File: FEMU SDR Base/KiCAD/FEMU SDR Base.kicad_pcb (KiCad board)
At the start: 4 copper layers, 164.8 x 186.6 mm, 71 parts, among them P1 Battery, P10 PWM2, P11 PWM3, P12 PWM4, P13 PWM1, P14 PWM2, P15 PWM3, P16 PWM4, P17 12V, P18 GND, P19 12V, P2 SDR_Shield_1, P20 GND, P21 S0GND, P22 S1GND, P23 S0DN, P24 S1DN, P25 S0DP, P26 S1DP, P27 PWM0, P28 PWM5, P29 PWM6, P3 SDR_Shield_2, P30 PWM7, P31 PWM0, P32 PWM5, P33 PWM6, P34 PWM7, P35 Battery, P4 12V, P5 GND, P6 12V, P7 GND, P8 Raspi_Power_Shield, P9 PWM1, U1 TPS562209, U2 LP38858-LDO, U3 LP38858-LDO, U4 7833, U5 7833

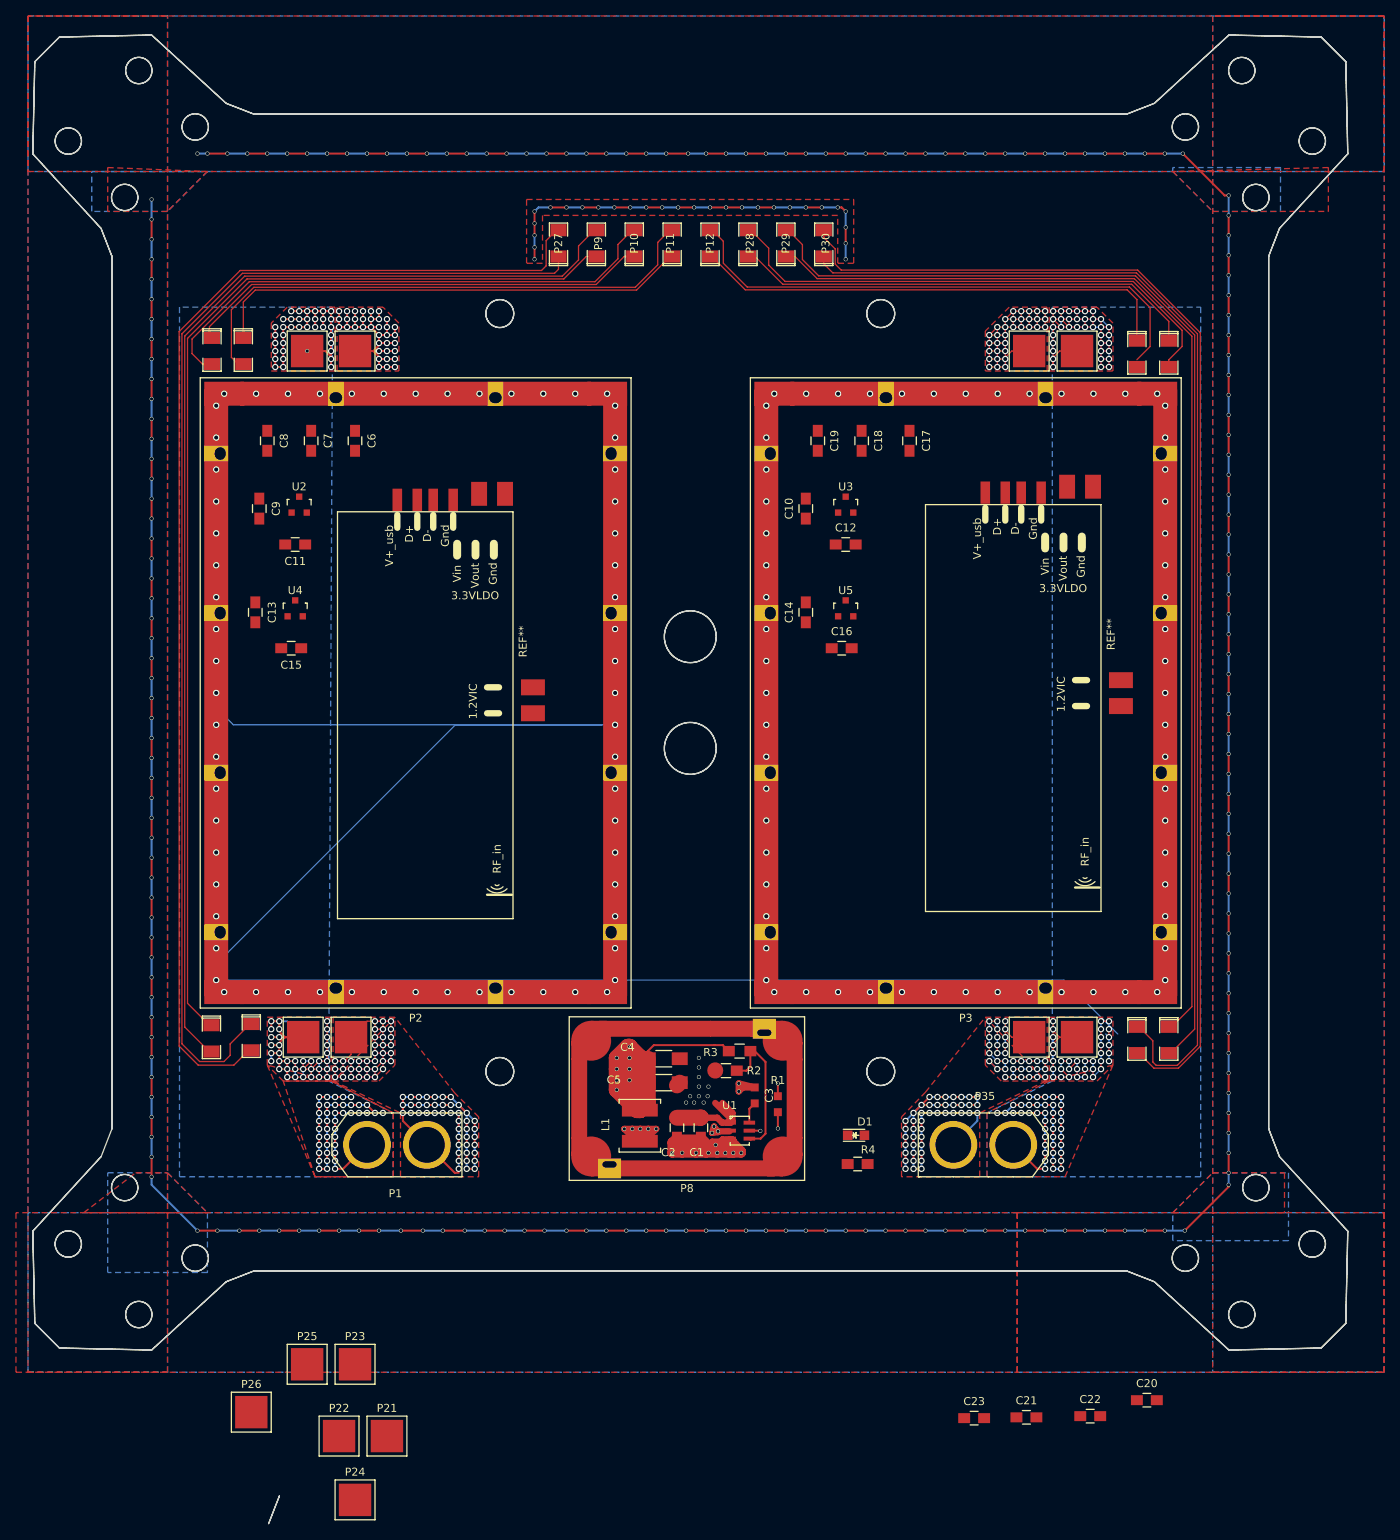
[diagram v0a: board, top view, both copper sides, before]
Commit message: Added esc mounts, power headers and usb headers
Signed-off-by: hardiepienaar <hardiepienaar@gmail.com>
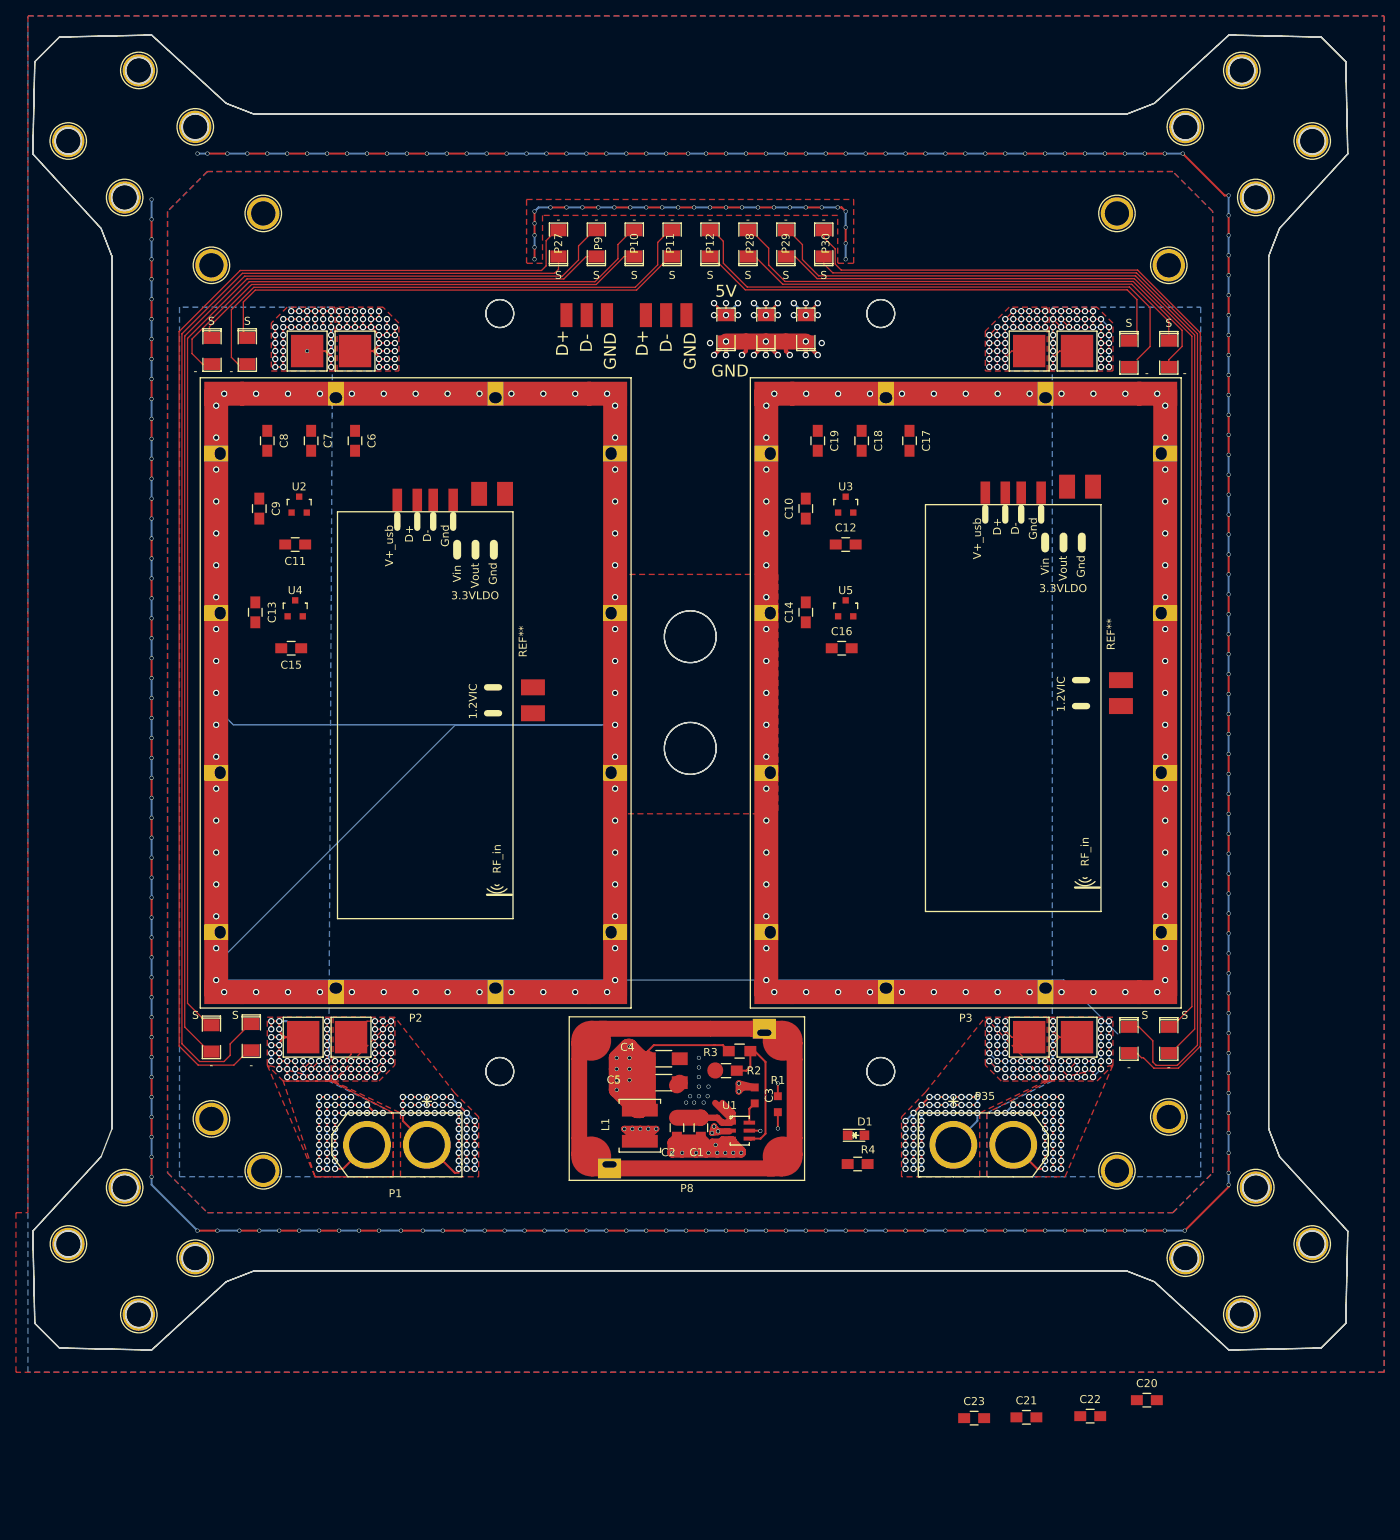
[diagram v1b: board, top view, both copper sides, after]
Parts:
- removed P23: S0DN, SMD_Packages:1Pin
- removed P24: S1DN, SMD_Packages:1Pin
- removed P25: S0DP, SMD_Packages:1Pin
- removed P26: S1DP, SMD_Packages:1Pin
- added M1: M1, Connect:1pin, F.Cu at (13.6, 146.6)
- added M10: M1, Connect:1pin, F.Cu at (6.55, 15.4)
- added M11: M1, Connect:1pin, F.Cu at (22.5, 13.7)
- added M12: M1, Connect:1pin, F.Cu at (13.6, 22.5)
- added M13: M1, Connect:1pin, F.Cu at (153.7, 6.58)
- added M14: M1, Connect:1pin, F.Cu at (146.6, 13.7)
- added M15: M1, Connect:1pin, F.Cu at (162.5, 15.4)
- added M16: M1, Connect:1pin, F.Cu at (155.4, 22.5)
- added M2: M1, Connect:1pin, F.Cu at (155.4, 146.6)
- added M3: M1, Connect:1pin, F.Cu at (162.5, 153.7)
- added M4: M1, Connect:1pin, F.Cu at (153.7, 162.5)
- added M5: M1, Connect:1pin, F.Cu at (146.6, 155.4)
- added M6: M1, Connect:1pin, F.Cu at (6.58, 153.7)
- added M7: M1, Connect:1pin, F.Cu at (15.4, 162.5)
- added M8: M1, Connect:1pin, F.Cu at (22.5, 155.4)
- added M9: M1, Connect:1pin, F.Cu at (15.4, 6.58)
- added P36: RPi, SMD_Packages:SMD-1206_Pol, F.Cu at (99.0, 38.9)
- added P37: PXH, SMD_Packages:SMD-1206_Pol, F.Cu at (94.0, 38.9)
- added P38: Rx, SMD_Packages:SMD-1206_Pol, F.Cu at (89.0, 38.9)
- added REF**: 1pin, Connect:1pin, F.Cu at (24.5, 31.0)
- added REF**: 1pin, Connect:1pin, F.Cu at (24.5, 138.0)
- added REF**: 1pin, Connect:1pin, F.Cu at (31.0, 24.5)
- added REF**: 1pin, Connect:1pin, F.Cu at (144.5, 31.0)
- added REF**: 1pin, Connect:1pin, F.Cu at (138.0, 24.5)
- added REF**: 1pin, Connect:1pin, F.Cu at (144.5, 137.8)
- added REF**: 1pin, Connect:1pin, F.Cu at (138.0, 144.5)
- added REF**: 1pin, Connect:1pin, F.Cu at (31.0, 144.5)
- P21: value S0GND -> SDR0; footprint SMD_Packages:1Pin -> Misc footprints:USB
- P22: value S1GND -> SDR1; footprint SMD_Packages:1Pin -> Misc footprints:USB
- moved P22 146.4 mm to (81.5, 37.2)
- moved P21 142.7 mm to (71.5, 37.2)
- moved P16 1.00 mm to (139.5, 42.1)
- moved P34 1.00 mm to (139.5, 128.1)
- moved P15 0.50 mm to (29.0, 41.8)
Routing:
- net +5V: track 95.7 -> 220.8 mm, vias 8 -> 22
- net GND: track 1642.1 -> 1668.3 mm, vias 587 -> 605
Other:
- board size 164.8 x 186.6 mm -> 164.8 x 164.8 mm
- board text added: "+"
- board text added: "-"
- board text added: "5V"
- board text added: "Connect 5V line (Antheun) Add feedthroughs (Antheun) Add usb isolation (Antheun) Finish SDR layouts (Antheun) Add MESA logo Add FEMU logo Add Description Add Rev and date Add Sneaky signitures Add mechanical drawings to silkscreen"
- board text added: "D+"
- board text added: "D-"
- board text added: "GND"
- board text added: "S"
- board text removed: "Add raspi power Add pixhawk pwr Add feedthroughs Add usb isolation Add esc wire strap mounts Add SMA grounding rings Add arm grounding rings"

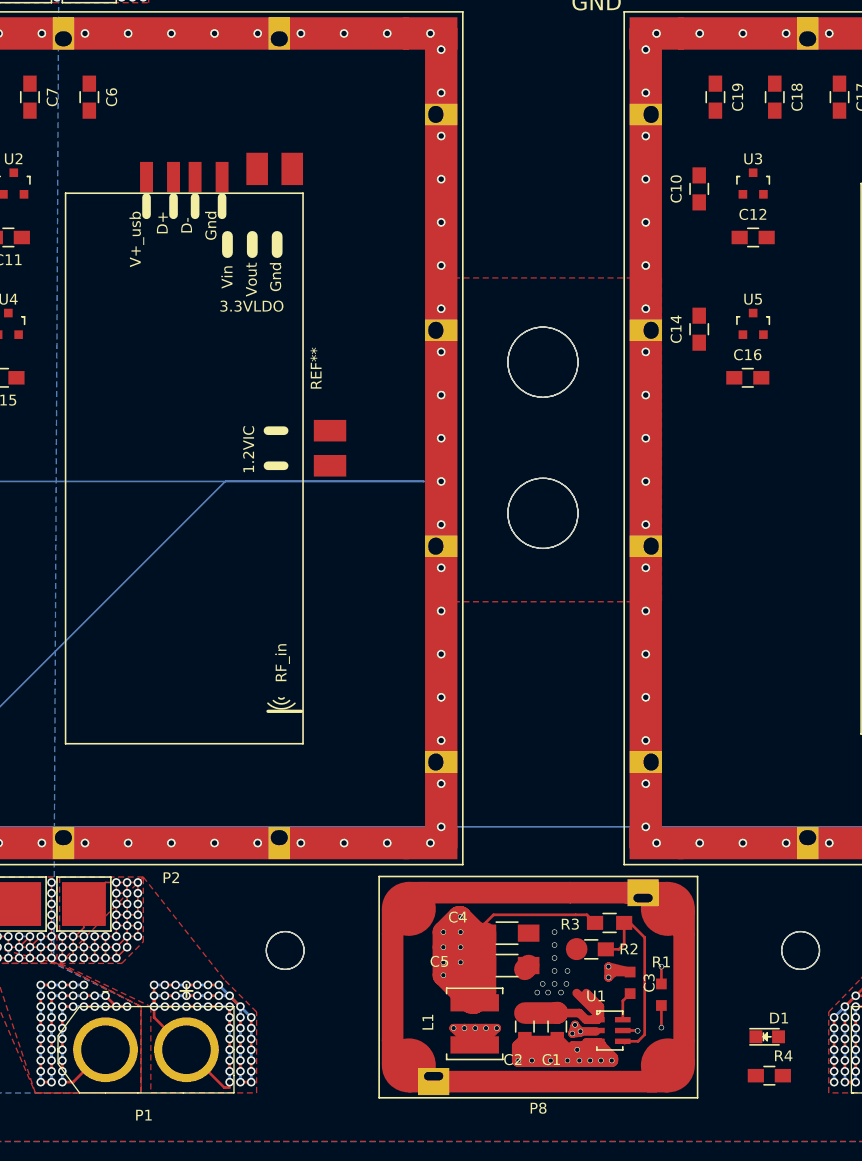
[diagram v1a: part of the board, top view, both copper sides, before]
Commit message: Added Stitching to RasPi PSU and finished this layout, added feedthrough and CM filter foots
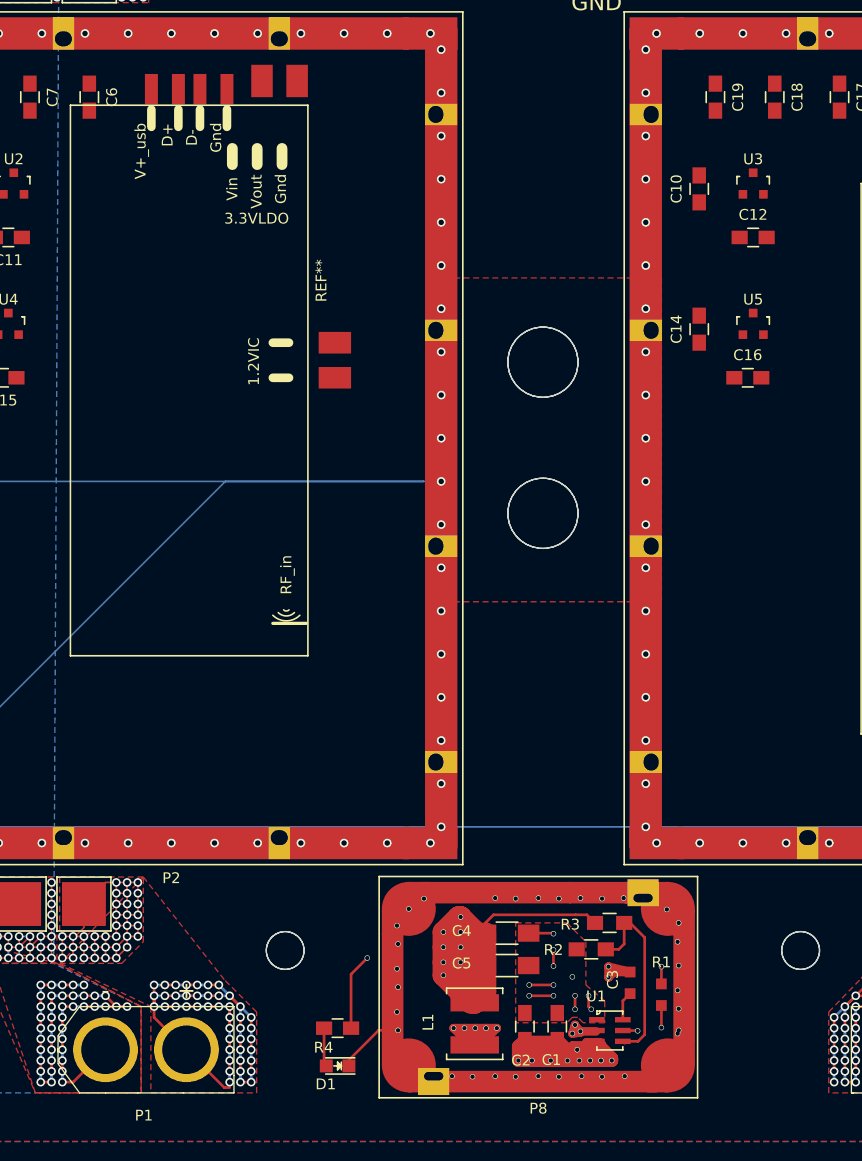
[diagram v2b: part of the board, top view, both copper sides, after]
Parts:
- moved R4 40.2 mm to (65.5, 139.2), turned to 180 degrees
- moved D1 39.9 mm to (65.5, 142.8), turned to 180 degrees
- moved REF** 8.16 mm to (40.8, 104.8)
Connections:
- D1 pad 1: Net-(D1-Pad1) -> GND
- R2 pad 2: Net-(D1-Pad1) -> Net-(R2-Pad2)
- R3 pad 2: Net-(D1-Pad1) -> Net-(R2-Pad2)
- U1 pad 4: Net-(D1-Pad1) -> Net-(R2-Pad2)
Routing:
- net GND: track 1668.3 -> 1748.0 mm, vias 605 -> 649
- net +5V: track 220.8 -> 240.7 mm, vias 22 -> 23
- net Net-(R2-Pad2): track 0.00 -> 17.9 mm
- net Net-(D1-Pad1): track 17.9 -> 0.00 mm
- net Net-(D1-Pad2): track 0.00 -> 3.87 mm
- net (no net): track 0.20 -> 0.00 mm, vias 11 -> 0
